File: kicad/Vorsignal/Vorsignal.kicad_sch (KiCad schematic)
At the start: 7 parts, among them J0 VCC, J1 VkzBw, J3 GELB, J4 GRÜN

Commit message: Add CC-BY-SA 4.0 license
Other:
- title: (none) -> KS-Vorsignal
- moved on the sheet: D1, D3, D5, J0, J1, J3, J4

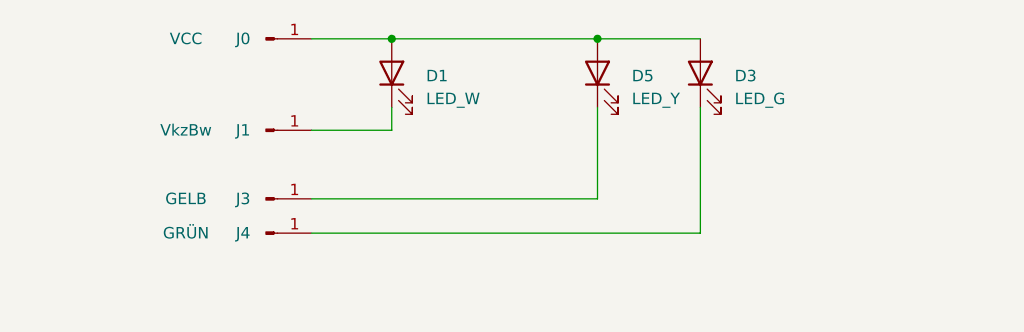
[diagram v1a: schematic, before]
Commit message: feat(VS): Add pre-signal repeater light
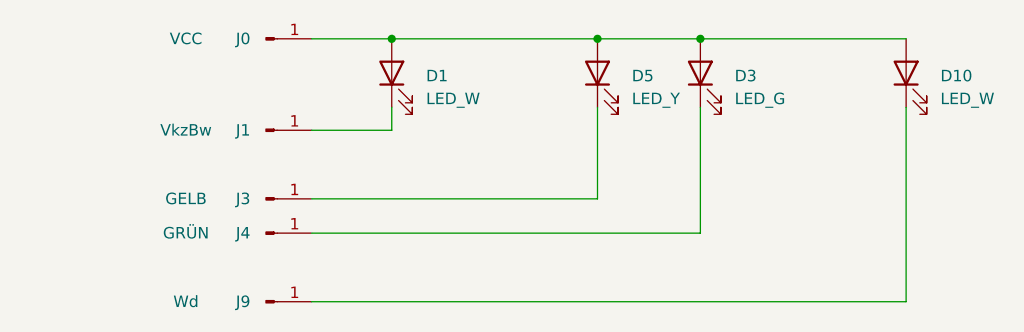
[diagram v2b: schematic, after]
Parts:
- added D10: LED_W, LED_SMD:LED_0402_1005Metric, symbol Device:LED
- added J9: Wd, Connector_Wire:SolderWirePad_1x01_SMD_1x2mm, symbol Connector:Conn_01x01_Male
- D1: LCSC C268305 -> C189305
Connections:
- net at D1.2 (A), D3.2 (A), D5.2 (A)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: now also D10.2 (A)
- new net: D10.1 (K), J9.1 (Pin_1)
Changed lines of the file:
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@@
   (title_block
     (title "KS-Vorsignal")
-    (date "2023-12-17")
-    (rev "1.0")
+    (date "2024-01-07")
+    (rev "2.0")
   )
   (junction (at 93.98 54.61) (diameter 0) (color 0 0 0 0)
@@
   (junction (at 116.84 54.61) (diameter 0) (color 0 0 0 0)
   )
+  (junction (at 128.27 54.61) (diameter 0) (color 0 0 0 0)
+  )
   (wire (pts (xy 85.09 64.77) (xy 93.98 64.77))
     (stroke (width 0) (type default))
@@
     (stroke (width 0) (type default))
   )
+  (wire (pts (xy 85.09 83.82) (xy 151.13 83.82))
+    (stroke (width 0) (type default))
+  )
   (wire (pts (xy 116.84 54.61) (xy 128.27 54.61))
     (stroke (width 0) (type default))
@@
     (stroke (width 0) (type default))
   )
+  (wire (pts (xy 151.13 83.82) (xy 151.13 62.23))
+    (stroke (width 0) (type default))
+  )
   (wire (pts (xy 93.98 54.61) (xy 116.84 54.61))
     (stroke (width 0) (type default))
@@
     (stroke (width 0) (type default))
   )
+  (wire (pts (xy 128.27 54.61) (xy 151.13 54.61))
+    (stroke (width 0) (type default))
+  )
   (wire (pts (xy 93.98 62.23) (xy 93.98 64.77))
     (stroke (width 0) (type default))
+  )
+  (symbol (lib_id "Device:LED") (at 151.13 58.42 90) (unit 1)
+    (in_bom yes) (on_board yes) (dnp no) (fields_autoplaced)
+    (property "Reference" "D10" (at 154.94 58.7375 90)
+      (effects (font (size 1.27 1.27)) (justify right))
+    )
+    (property "Value" "LED_W" (at 154.94 61.2775 90)
+      (effects (font (size 1.27 1.27)) (justify right))
+    )
+    (property "Footprint" "LED_SMD:LED_0402_1005Metric" (at 151.13 58.42 0)
+      (effects (font (size 1.27 1.27)) hide)
+    )
+    (property "Datasheet" "~" (at 151.13 58.42 0)
+      (effects (font (size 1.27 1.27)) hide)
+    )
+    (property "LCSC" "C189305" (at 154.94 58.7374 0)
+      (effects (font (size 1.27 1.27)) hide)
+    )
+    (pin "1")
+    (pin "2")
+    (instances
+      (project "Vorsignal"
+        (path "/e63e39d7-6ac0-4ffd-8aa3-1841a4541b55"
+          (reference "D10") (unit 1)
+        )
+      )
+    )
   )
   (symbol (lib_id "Connector:Conn_01x01_Male") (at 80.01 64.77 0) (unit 1)
@@
       (effects (font (size 1.27 1.27)) hide)
     )
-    (property "LCSC" "C268305" (at 97.79 58.7374 0)
+    (property "LCSC" "C189305" (at 97.79 58.7374 0)
       (effects (font (size 1.27 1.27)) hide)
     )
@@
         )
       )
+    )
+  )
+  (symbol (lib_id "Connector:Conn_01x01_Male") (at 80.01 83.82 0) (unit 1)
+    (in_bom no) (on_board yes) (dnp no)
+    (property "Reference" "J9" (at 77.47 83.82 0)
+      (effects (font (size 1.27 1.27)))
+    )
+    (property "Value" "Wd" (at 71.12 83.82 0)
+      (effects (font (size 1.27 1.27)))
+    )
+    (property "Footprint" "Connector_Wire:SolderWirePad_1x01_SMD_1x2mm" (at 80.01 83.82 0)
+      (effects (font (size 1.27 1.27)) hide)
+    )
+    (property "Datasheet" "~" (at 80.01 83.82 0)
+      (effects (font (size 1.27 1.27)) hide)
+    )
+    (pin "1")
+    (instances
+      (project "Vorsignal"
+        (path "/e63e39d7-6ac0-4ffd-8aa3-1841a4541b55"
+          (reference "J9") (unit 1)
+        )
+      )
